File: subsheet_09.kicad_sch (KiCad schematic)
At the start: 0 parts

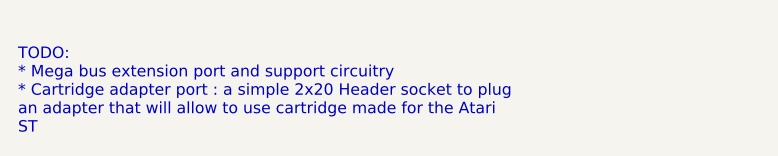
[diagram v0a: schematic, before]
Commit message: added todo in schematics
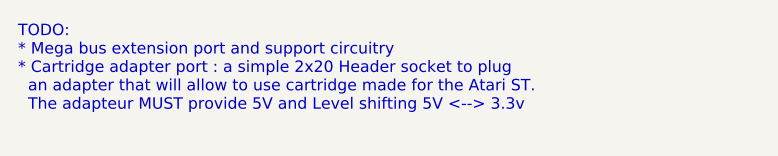
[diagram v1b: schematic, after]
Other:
- note added: "TODO: * Mega bus extension port and support circuitry * Cartridge adapter port : a simple 2x20 Header socket to plug an adapter that will allow to use cartridge made for the Atari ST. The adapteur MUST provide 5V and Level shifting 5V <--> 3.3v"
- note removed: "TODO: * Mega bus extension port and support circuitry * Cartridge adapter port : a simple 2x20 Header socket to plug an adapter that will allow to use cartridge made for the Atari ST"
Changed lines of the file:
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@@
     (comment 4 "Original repository :")
   )
-  (text "TODO:\n* Mega bus extension port and support circuitry\n* Cartridge adapter port : a simple 2x20 Header socket to plug\nan adapter that will allow to use cartridge made for the Atari\nST"
-    (at 21.59 27.94 0)
+  (text "TODO:\n* Mega bus extension port and support circuitry\n* Cartridge adapter port : a simple 2x20 Header socket to plug\n  an adapter that will allow to use cartridge made for the Atari ST.\n  The adapteur MUST provide 5V and Level shifting 5V <--> 3.3v"
+    (at 21.59 25.4 0)
     (effects (font (size 1.27 1.27)) (justify left bottom))
   )
